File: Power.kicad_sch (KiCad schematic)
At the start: 15 parts

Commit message: Original V2 Update
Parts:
- added C16: 10 uF, Capacitor_THT:C_Radial_D6.3mm_H11.0mm_P2.50mm, symbol Device:C_Polarized_US
- added L3: 10 uH, BRG_Footprints:SBT0210, symbol Device:L
- C10: renamed from C1; value (none) -> 10 uF; footprint (none) -> Capacitor_THT:C_Rect_L13.5mm_W5.0mm_P10.00mm_FKS3_FKP3_MKS4; Mouser Part Number 661-KTD101B106M80A0B -> 810-CGA9N3X7S2A106KS
- C11: renamed from C2; value (none) -> 10 uF; footprint (none) -> Capacitor_THT:C_Rect_L13.5mm_W5.0mm_P10.00mm_FKS3_FKP3_MKS4; Mouser Part Number 661-KTD101B106M80A0B -> 810-CGA9N3X7S2A106KS
- C12: renamed from C3; value (none) -> 2.2 uF; footprint (none) -> Capacitor_SMD:C_0805_2012Metric_Pad1.18x1.45mm_HandSolder; Mouser Part Number 810-CGA4J1X8L225125C -> 81-GRM21BD72A225KE01L
- C13: renamed from C4; value (none) -> 2.2 uF; footprint (none) -> Capacitor_SMD:C_0805_2012Metric_Pad1.18x1.45mm_HandSolder; Mouser Part Number 810-CGA4J1X8L225125C -> 81-GRM21BD72A225KE01L
- C14: renamed from C5; value (none) -> 0.1uF; footprint (none) -> Capacitor_SMD:C_0805_2012Metric_Pad1.18x1.45mm_HandSolder
- C15: renamed from C6; value (none) -> 0.1uF; footprint (none) -> Capacitor_SMD:C_0805_2012Metric_Pad1.18x1.45mm_HandSolder
- D1: value (none) -> Red LED; footprint (none) -> LED_THT:LED_D3.0mm
- J6: renamed from J1; value (none) -> Barrel_Jack_Switch; footprint (none) -> BRG_Footprints:PJ-102AH
- J7: value (none) -> Conn_01x03; footprint (none) -> Connector_PinHeader_2.54mm:PinHeader_1x03_P2.54mm_Vertical
- L1, L2: value (none) -> 68 uH; footprint (none) -> Inductor_SMD:L_Taiyo-Yuden_NR-60xx_HandSoldering; Mouser Part Number 963-NR5040T6R8M -> 963-NRS6012T680MMGJ
- R2: renamed from R1; value (none) -> 680; footprint (none) -> Resistor_SMD:R_0805_2012Metric_Pad1.20x1.40mm_HandSolder
- S1: value (none) -> On/Off Switch; footprint (none) -> BRG_Footprints:SW_1101M2S3CQE2
- T1: value (none) -> R-78E5.0-1.0; footprint (none) -> BRG_Footprints:R-78E5.0-1.0
- T2: value (none) -> R-78E3.3-1.0; footprint (none) -> BRG_Footprints:R-78E3.3-1.0
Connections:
- net +3V3: now also L3.1; no longer J7.3 (Pin_3)
- net GND: now also C16.2
- new net PWR_3.3v: C16.1, J7.3 (Pin_3), L3.2
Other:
- title: (none) -> AVR Prototype Board

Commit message: Routed by FreeRouting
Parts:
- C10, C11: footprint Capacitor_THT:C_Rect_L13.5mm_W5.0mm_P10.00mm_FKS3_FKP3_MKS4 -> Capacitor_SMD:C_2220_5650Metric_Pad1.97x5.40mm_HandSolder
- C16: Mouser Part Number 80-ESK106M100AE3EA -> 667-ECA-2AM100
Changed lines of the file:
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@@
       (effects (font (size 1.27 1.27)) (justify left))
     )
-    (property "Footprint" "Capacitor_THT:C_Rect_L13.5mm_W5.0mm_P10.00mm_FKS3_FKP3_MKS4" (id 2) (at 82.2452 74.93 0)
+    (property "Footprint" "Capacitor_SMD:C_2220_5650Metric_Pad1.97x5.40mm_HandSolder" (id 2) (at 82.2452 74.93 0)
       (effects (font (size 1.27 1.27)) hide)
     )
@@
       (effects (font (size 1.27 1.27)) (justify left))
     )
-    (property "Footprint" "Capacitor_THT:C_Rect_L13.5mm_W5.0mm_P10.00mm_FKS3_FKP3_MKS4" (id 2) (at 82.2452 118.11 0)
+    (property "Footprint" "Capacitor_SMD:C_2220_5650Metric_Pad1.97x5.40mm_HandSolder" (id 2) (at 82.2452 118.11 0)
       (effects (font (size 1.27 1.27)) hide)
     )
@@
       (effects (font (size 1.27 1.27)) hide)
     )
-    (property "Mouser Part Number" "80-ESK106M100AE3EA" (id 4) (at 173.99 114.3 0)
-      (effects (font (size 1.27 1.27)) hide)
-    )
+    (property "Mouser Part Number" "667-ECA-2AM100" (id 4) (at 173.99 114.3 0)
+      (effects (font (size 1.27 1.27)) hide)
+    )

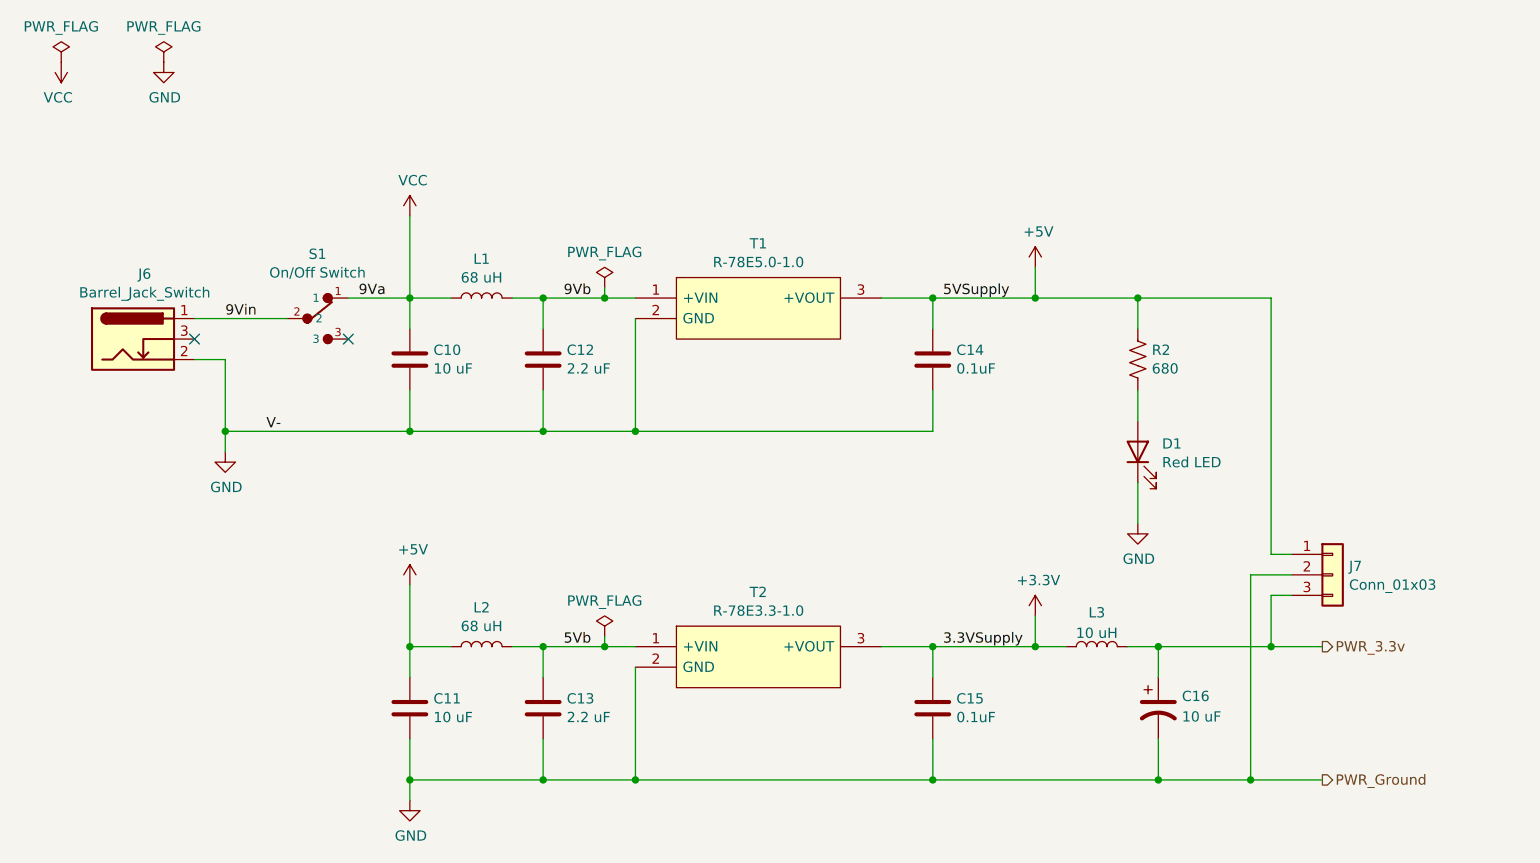
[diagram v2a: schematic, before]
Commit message: Updated V3.3 Converter to VCC input
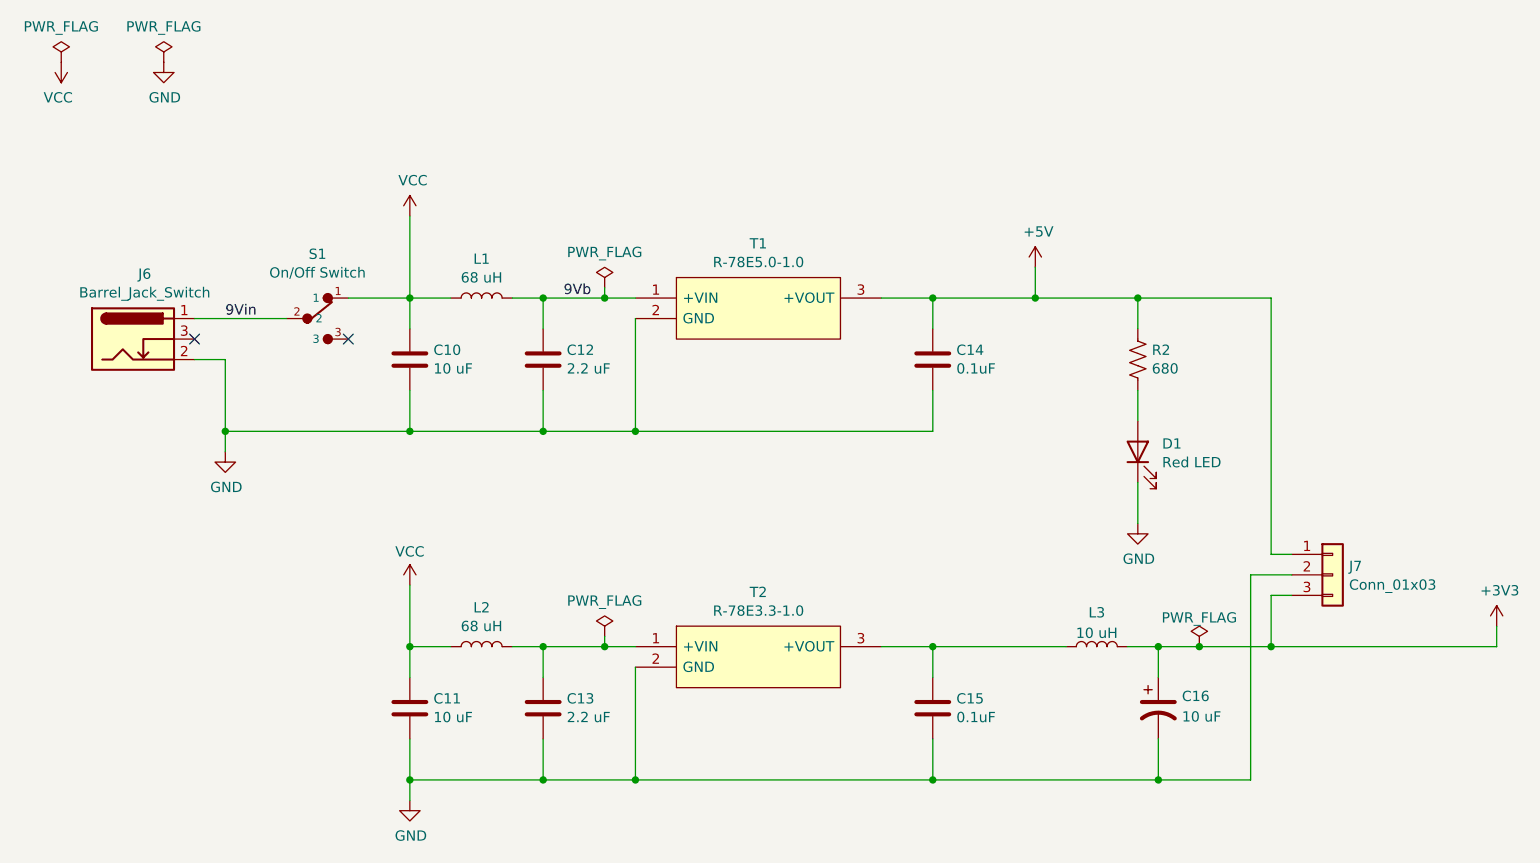
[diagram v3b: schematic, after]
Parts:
- C10, C11: footprint Capacitor_SMD:C_2220_5650Metric_Pad1.97x5.40mm_HandSolder -> Capacitor_SMD:C_2220_5750Metric_Pad1.97x5.40mm_HandSolder; Manufacturer_Part_Number KTD101B106M80A0B -> A004
- C12, C13: Manufacturer_Part_Number CGA4J1X8L1V225K125AC -> A003
- C14, C15: Manufacturer_Part_Number C0805C104J5RAUTO -> A002
- C16: footprint Capacitor_THT:C_Radial_D6.3mm_H11.0mm_P2.50mm -> Capacitor_THT:C_Radial_D5.0mm_H11.0mm_P2.00mm; Manufacturer_Part_Number (none) -> B102
- D1: Manufacturer_Part_Number TLHK46Q1R2 -> B103
- J6: Manufacturer_Part_Number PJ-102AH -> B108
- J7: Manufacturer_Part_Number (none) -> B109
- L1, L2: Manufacturer_Part_Number NR5040T6R8M -> A006
- L3: Manufacturer_Part_Number (none) -> B111
- R2: Manufacturer_Part_Number RC0805FR-13680RL -> A007
- S1: Description_1 (none) -> SPDT Slide Switch; Manufacturer_Part_Number 1101M2S3CQE2 -> B112
- T1: Description_1 (none) -> Non-Isolated DC/DC Converters 8-28Vin 5V 1.0A THRU
- T2: Description_1 (none) -> Non-Isolated DC/DC Converters 8-28Vin 3.3V 1.0A THRU
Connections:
- net PWR_3.3v is gone; now on net +3V3: C16.1, J7.3 (Pin_3), L3.2
- net +3V3: no longer C15.1, L3.1, T2.3 (+VOUT)
- net +5V: no longer C11.1, L2.1
- net VCC: now also C11.1, L2.1
- net 5Vb: no longer names the net of C13.1, L2.2, T2.1 (+VIN)
- new net: C15.1, L3.1, T2.3 (+VOUT)
